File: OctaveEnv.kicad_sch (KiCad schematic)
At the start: 89 parts, among them J101 IN, J102 PWR, J103 OUT, Q101 BC857, SW101 Stomp, U101 AZ34063U, U102 L7805, U103 TL074, U104 74HCT74, U105 LM13700, U106 TL074, U107 TL072

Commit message: rev1 sent to fab
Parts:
- added TP108: SWC, TestPoint:TestPoint_THTPad_D1.5mm_Drill0.7mm_VAL, symbol Connector:TestPoint
- added TP109: SWE, TestPoint:TestPoint_THTPad_D1.5mm_Drill0.7mm_VAL, symbol Connector:TestPoint
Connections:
- net SWC: now reaches R102.2, U101.1 (SWC), U101.7 (Sense), U101.8 (DRC)
- net SWC: now also TP108.1
- net SWE: now reaches D102.1 (K), L101.1, U101.2 (SWE)
- net SWE: now also TP109.1
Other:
- moved on the sheet: L101
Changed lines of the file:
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@@
 	)
 	(junction
-		(at 369.062 161.798)
-		(diameter 0)
-		(color 0 0 0 0)
-	)
-	(junction
 		(at 200.406 202.692)
 		(diameter 0)
@@
 	)
 	(junction
+		(at 371.348 161.798)
+		(diameter 0)
+		(color 0 0 0 0)
+	)
+	(junction
 		(at 69.85 111.252)
 		(diameter 0)
@@
 	(wire
 		(pts
+			(xy 97.536 254) (xy 97.536 256.286)
+		)
+		(stroke
+			(width 0)
+			(type default)
+		)
+	)
+	(wire
+		(pts
 			(xy 281.432 226.314) (xy 281.432 227.076)
 		)
@@
 	(wire
 		(pts
-			(xy 378.206 161.798) (xy 378.206 162.814)
+			(xy 383.286 161.798) (xy 383.286 162.814)
 		)
 		(stroke
@@
 	(wire
 		(pts
-			(xy 369.062 166.878) (xy 369.062 161.798)
+			(xy 371.348 166.878) (xy 371.348 161.798)
 		)
 		(stroke
@@
 	(wire
 		(pts
-			(xy 367.284 161.798) (xy 369.062 161.798)
+			(xy 367.284 161.798) (xy 371.348 161.798)
 		)
 		(stroke
@@
 	(wire
 		(pts
-			(xy 369.062 161.798) (xy 370.586 161.798)
+			(xy 177.038 117.348) (xy 177.038 125.984)
 		)
 		(stroke
@@
 	(wire
 		(pts
-			(xy 177.038 117.348) (xy 177.038 125.984)
+			(xy 367.284 148.336) (xy 328.168 148.336)
 		)
 		(stroke
@@
 	(wire
 		(pts
-			(xy 367.284 148.336) (xy 328.168 148.336)
+			(xy 34.036 61.468) (xy 34.036 62.484)
 		)
 		(stroke
@@
 	(wire
 		(pts
-			(xy 34.036 61.468) (xy 34.036 62.484)
+			(xy 164.084 106.934) (xy 163.068 106.934)
 		)
 		(stroke
@@
 	(wire
 		(pts
-			(xy 164.084 106.934) (xy 163.068 106.934)
+			(xy 59.69 164.592) (xy 66.548 164.592)
 		)
 		(stroke
@@
 	(wire
 		(pts
-			(xy 59.69 164.592) (xy 66.548 164.592)
+			(xy 122.428 180.086) (xy 120.65 180.086)
 		)
 		(stroke
@@
 	(wire
 		(pts
-			(xy 122.428 180.086) (xy 120.65 180.086)
+			(xy 41.148 111.252) (xy 46.228 111.252)
 		)
 		(stroke
@@
 	(wire
 		(pts
-			(xy 41.148 111.252) (xy 46.228 111.252)
+			(xy 371.348 161.798) (xy 375.666 161.798)
 		)
 		(stroke
@@
 	(wire
 		(pts
+			(xy 107.442 254.254) (xy 107.442 256.54)
+		)
+		(stroke
+			(width 0)
+			(type default)
+		)
+	)
+	(wire
+		(pts
 			(xy 245.618 227.838) (xy 245.618 228.854)
 		)
@@
 	(wire
 		(pts
-			(xy 383.794 166.878) (xy 369.062 166.878)
+			(xy 383.794 166.878) (xy 371.348 166.878)
 		)
 		(stroke
@@
 	(rectangle
 		(start 29.718 230.378)
-		(end 97.282 265.176)
+		(end 121.412 265.176)
 		(stroke
 			(width 0)
@@
 		)
 	)
+	(label "SWC"
+		(at 367.284 148.336 0)
+		(fields_autoplaced yes)
+		(effects
+			(font
+				(size 1.27 1.27)
+			)
+			(justify left bottom)
+		)
+	)
 	(label "OCT_VCA"
 		(at 241.046 94.488 180)
@@
 		)
 	)
+	(label "SWE"
+		(at 371.348 161.798 0)
+		(fields_autoplaced yes)
+		(effects
+			(font
+				(size 1.27 1.27)
+			)
+			(justify left bottom)
+		)
+	)
 	(label "Edge"
 		(at 67.564 256.032 0)
@@
 		)
 	)
+	(label "SWE"
+		(at 107.442 256.54 0)
+		(fields_autoplaced yes)
+		(effects
+			(font
+				(size 1.27 1.27)
+			)
+			(justify left bottom)
+		)
+	)
 	(label "SQR1"
 		(at 76.708 256.286 0)
@@
 		)
 	)
+	(label "SWC"
+		(at 97.536 256.286 0)
+		(fields_autoplaced yes)
+		(effects
+			(font
+				(size 1.27 1.27)
+			)
+			(justify left bottom)
+		)
+	)
 	(global_label "ENV"
 		(shape output)
@@
 	)
 	(symbol
+		(lib_id "Connector:TestPoint")
+		(at 97.536 254 0)
+		(unit 1)
+		(exclude_from_sim no)
+		(in_bom no)
+		(on_board yes)
+		(dnp no)
+		(fields_autoplaced yes)
+		(property "Reference" "TP108"
+			(at 99.06 249.4279 0)
+			(effects
+				(font
+					(size 1.27 1.27)
+				)
+				(justify left)
+			)
+		)
+		(property "Value" "SWC"
+			(at 99.06 251.9679 0)
+			(effects
+				(font
+					(size 1.27 1.27)
+				)
+				(justify left)
+			)
+		)
+		(property "Footprint" "TestPoint:TestPoint_THTPad_D1.5mm_Drill0.7mm_VAL"
+			(at 102.616 254 0)
+			(effects
+				(font
+					(size 1.27 1.27)
+				)
+				(hide yes)
+			)
+		)
+		(property "Datasheet" "~"
+			(at 102.616 254 0)
+			(effects
+				(font
+					(size 1.27 1.27)
+				)
+				(hide yes)
+			)
+		)
+		(property "Description" "test point"
+			(at 97.536 254 0)
+			(effects
+				(font
+					(size 1.27 1.27)
+				)
+				(hide yes)
+			)
+		)
+		(pin "1"
+		)
+		(instances
+			(project "OctaveEnv"
+				(path "/d758546a-c7ec-4cba-b958-982db76e9349"
+					(reference "TP108")
+					(unit 1)
+				)
+			)
+		)
+	)
+	(symbol
 		(lib_id "Regulator_Linear:L7805")
 		(at 355.854 222.504 0)
@@
 	(symbol
 		(lib_id "Device:L")
-		(at 374.396 161.798 90)
+		(at 379.476 161.798 90)
 		(unit 1)
 		(exclude_from_sim no)
@@
 		(fields_autoplaced yes)
 		(property "Reference" "L101"
-			(at 374.396 156.464 90)
+			(at 379.476 156.464 90)
 			(effects
 				(font
@@
 		)
 		(property "Value" "68uH"
-			(at 374.396 159.004 90)
+			(at 379.476 159.004 90)
 			(effects
 				(font
@@
 		)
 		(property "Footprint" "Inductor_SMD:L_TDK_VLS6045EX_VLS6045AF"
-			(at 374.396 161.798 0)
+			(at 379.476 161.798 0)
 			(effects
 				(font
@@
 		)
 		(property "Datasheet" "~"
-			(at 374.396 161.798 0)
+			(at 379.476 161.798 0)
 			(effects
 				(font
@@
 		)
 		(property "Description" "Inductor"
-			(at 374.396 161.798 0)
+			(at 379.476 161.798 0)
 			(effects
 				(font
@@
 	)
 	(symbol
+		(lib_id "Connector:TestPoint")
+		(at 107.442 254.254 0)
+		(unit 1)
+		(exclude_from_sim no)
+		(in_bom no)
+		(on_board yes)
+		(dnp no)
+		(fields_autoplaced yes)
+		(property "Reference" "TP109"
+			(at 109.22 249.6819 0)
+			(effects
+				(font
+					(size 1.27 1.27)
+				)
+				(justify left)
+			)
+		)
+		(property "Value" "SWE"
+			(at 109.22 252.2219 0)
+			(effects
+				(font
+					(size 1.27 1.27)
+				)
+				(justify left)
+			)
+		)
+		(property "Footprint" "TestPoint:TestPoint_THTPad_D1.5mm_Drill0.7mm_VAL"
+			(at 112.522 254.254 0)
+			(effects
+				(font
+					(size 1.27 1.27)
+				)
+				(hide yes)
+			)
+		)
+		(property "Datasheet" "~"
+			(at 112.522 254.254 0)
+			(effects
+				(font
+					(size 1.27 1.27)
+				)
+				(hide yes)
+			)
+		)
+		(property "Description" "test point"
+			(at 107.442 254.254 0)
+			(effects
+				(font
+					(size 1.27 1.27)
+				)
+				(hide yes)
+			)
+		)
+		(pin "1"
+		)
+		(instances
+			(project "OctaveEnv"
+				(path "/d758546a-c7ec-4cba-b958-982db76e9349"
+					(reference "TP109")
+					(unit 1)
+				)
+			)
+		)
+	)
+	(symbol
 		(lib_id "power:+5V")
 		(at 137.922 48.768 0)
@@
 	(symbol
 		(lib_id "power:GND")
-		(at 378.206 162.814 0)
+		(at 383.286 162.814 0)
 		(unit 1)
 		(exclude_from_sim no)
@@
 		(fields_autoplaced yes)
 		(property "Reference" "#PWR0114"
-			(at 378.206 169.164 0)
+			(at 383.286 169.164 0)
 			(effects
 				(font
@@
 		)
 		(property "Value" "GND"
-			(at 378.206 166.624 0)
+			(at 383.286 166.624 0)
 			(effects
 				(font
@@
 		)
 		(property "Footprint" ""
-			(at 378.206 162.814 0)
+			(at 383.286 162.814 0)
 			(effects
 				(font
@@
 		)
 		(property "Datasheet" ""
-			(at 378.206 162.814 0)
+			(at 383.286 162.814 0)
 			(effects
 				(font
@@
 		)
 		(property "Description" "Power symbol creates a global label with name \"GND\" , ground"
-			(at 378.206 162.814 0)
+			(at 383.286 162.814 0)
 			(effects
 				(font

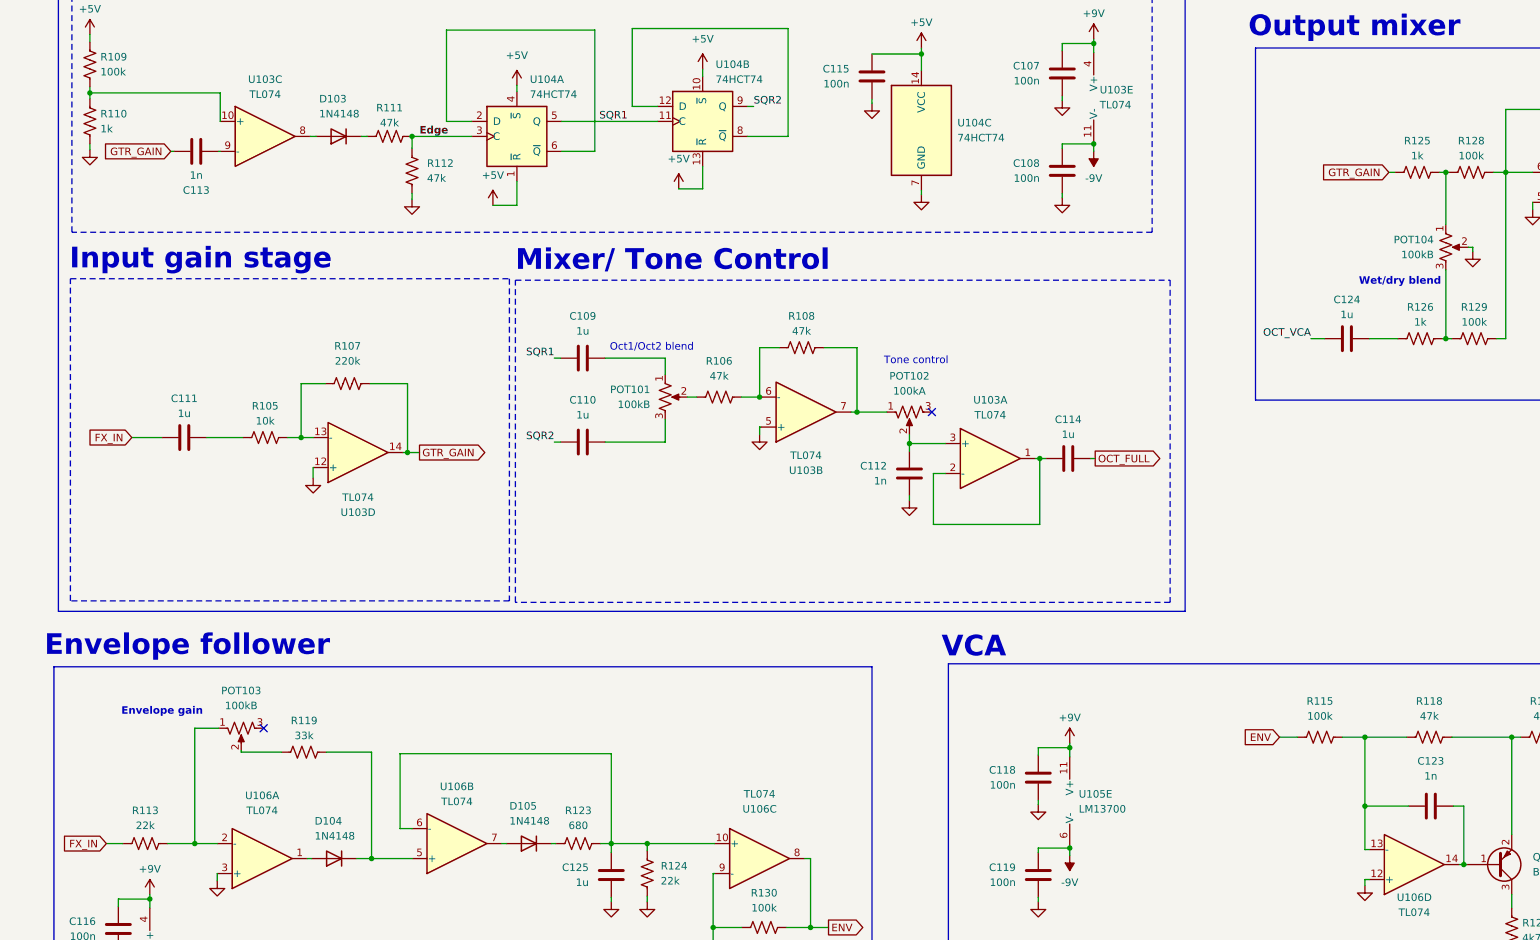
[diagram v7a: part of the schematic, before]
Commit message: octave up sim
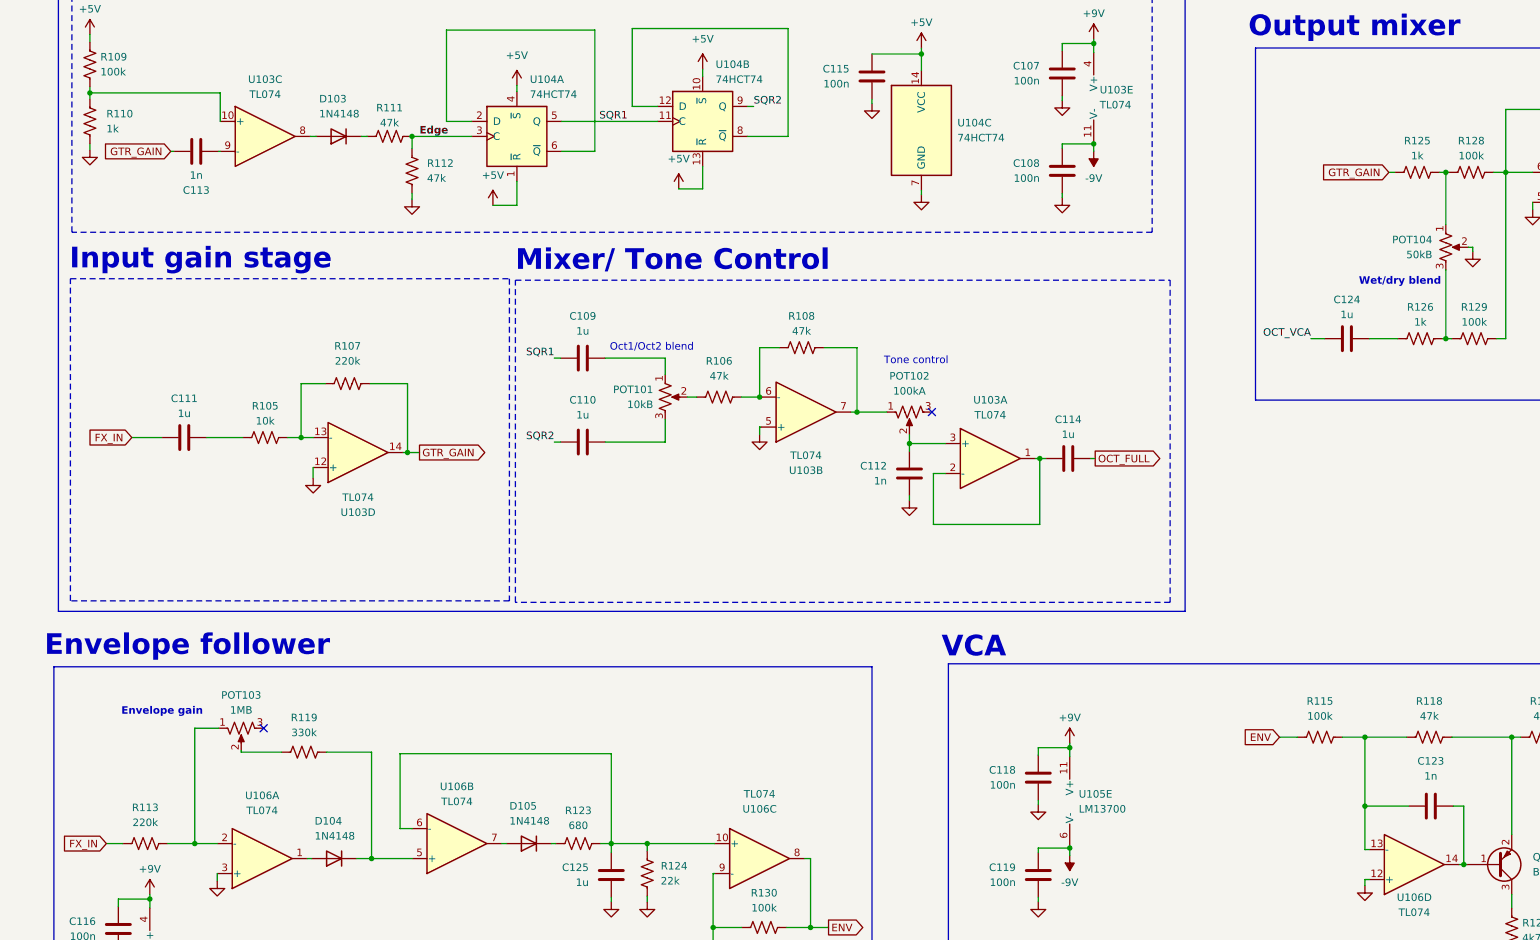
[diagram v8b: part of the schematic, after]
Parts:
- POT101: value 100kB -> 10kB
- POT103: value 100kB -> 1MB
- POT104: value 100kB -> 50kB
- R113: value 22k -> 220k
- R119: value 33k -> 330k
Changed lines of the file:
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@@
 		(fields_autoplaced yes)
 		(property "Reference" "POT103"
-			(at 59.69 154.178 90)
+			(at 59.69 154.94 90)
 			(effects
 				(font
@@
 			)
 		)
-		(property "Value" "100kB"
-			(at 59.69 156.718 90)
+		(property "Value" "1MB"
+			(at 59.69 157.48 90)
 			(effects
 				(font
@@
 		(fields_autoplaced yes)
 		(property "Reference" "R113"
-			(at 43.434 174.498 90)
+			(at 43.434 173.99 90)
 			(effects
 				(font
@@
 			)
 		)
-		(property "Value" "22k"
-			(at 43.434 177.038 90)
+		(property "Value" "220k"
+			(at 43.434 176.53 90)
 			(effects
 				(font
@@
 		(fields_autoplaced yes)
 		(property "Reference" "R110"
-			(at 35.814 56.3879 0)
+			(at 36.83 56.3879 0)
 			(effects
 				(font
@@
 		)
 		(property "Value" "1k"
-			(at 35.814 58.9279 0)
+			(at 36.83 58.9279 0)
 			(effects
 				(font
@@
 		(fields_autoplaced yes)
 		(property "Reference" "POT101"
-			(at 129.032 103.1239 0)
+			(at 129.54 103.1239 0)
 			(effects
 				(font
@@
 			)
 		)
-		(property "Value" "100kB"
-			(at 129.032 105.6639 0)
+		(property "Value" "10kB"
+			(at 129.54 105.6639 0)
 			(effects
 				(font
@@
 		(fields_autoplaced yes)
 		(property "Reference" "POT104"
-			(at 261.874 77.7239 0)
+			(at 261.62 77.7239 0)
 			(effects
 				(font
@@
 			)
 		)
-		(property "Value" "100kB"
-			(at 261.874 80.2639 0)
+		(property "Value" "50kB"
+			(at 261.62 80.2639 0)
 			(effects
 				(font
@@
 		(fields_autoplaced yes)
 		(property "Reference" "R119"
-			(at 70.358 159.258 90)
+			(at 70.358 158.75 90)
 			(effects
 				(font
@@
 			)
 		)
-		(property "Value" "33k"
-			(at 70.358 161.798 90)
+		(property "Value" "330k"
+			(at 70.358 161.29 90)
 			(effects
 				(font
